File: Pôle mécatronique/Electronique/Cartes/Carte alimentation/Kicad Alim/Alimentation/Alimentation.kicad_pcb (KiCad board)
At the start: 2 copper layers, 68.6 x 78.7 mm, 22 parts, among them J1 Conn_01x04, J2 Conn_01x04, J3 Conn_01x04, J4 Conn_01x05, J5 Conn_01x05, J6 Conn_02x03_Odd_Even, J7 Conn_02x10_Odd_Even, J8 Conn_01x02, J9 Conn_01x02, K1 G5LE-1, Q1 BD135, U1 TSR_2-2450, U2 TSR_2-2450, U3 TSR_2-24120

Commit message: Update HAT + commande
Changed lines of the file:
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@@
   (segment (start 132.842 62.388) (end 143.002 52.228) (width 0.6) (layer "B.Cu") (net 1))
   (segment (start 132.842 72.898) (end 132.842 62.388) (width 0.6) (layer "B.Cu") (net 1))
-  (segment (start 112.522 50.228) (end 104.902 50.228) (width 0.3) (layer "B.Cu") (net 2))
+  (segment (start 112.522 50.228) (end 104.902 50.228) (width 0.5) (layer "B.Cu") (net 2))
   (segment (start 102.172 50.228) (end 102.077 50.133) (width 0.3) (layer "B.Cu") (net 2))
-  (segment (start 134.112 50.228) (end 125.222 50.228) (width 0.3) (layer "B.Cu") (net 2))
-  (segment (start 144.462 50.228) (end 145.542 51.308) (width 0.3) (layer "B.Cu") (net 2))
+  (segment (start 134.112 50.228) (end 125.222 50.228) (width 0.5) (layer "B.Cu") (net 2))
+  (segment (start 144.462 50.228) (end 145.542 51.308) (width 0.5) (layer "B.Cu") (net 2))
   (segment (start 102.077 50.133) (end 97.917 50.133) (width 0.3) (layer "B.Cu") (net 2))
-  (segment (start 145.542 53.213) (end 145.542 51.308) (width 0.3) (layer "B.Cu") (net 2))
-  (segment (start 143.002 50.228) (end 144.462 50.228) (width 0.3) (layer "B.Cu") (net 2))
-  (segment (start 125.222 50.228) (end 112.522 50.228) (width 0.3) (layer "B.Cu") (net 2))
-  (segment (start 143.002 50.228) (end 134.112 50.228) (width 0.3) (layer "B.Cu") (net 2))
+  (segment (start 145.542 53.213) (end 145.542 51.308) (width 0.5) (layer "B.Cu") (net 2))
+  (segment (start 143.002 50.228) (end 144.462 50.228) (width 0.5) (layer "B.Cu") (net 2))
+  (segment (start 125.222 50.228) (end 112.522 50.228) (width 0.5) (layer "B.Cu") (net 2))
+  (segment (start 143.002 50.228) (end 134.112 50.228) (width 0.5) (layer "B.Cu") (net 2))
   (segment (start 102.172 50.228) (end 105.537 50.228) (width 0.3) (layer "B.Cu") (net 2))
-  (segment (start 137.922 72.898) (end 137.922 60.833) (width 0.3) (layer "B.Cu") (net 2))
-  (segment (start 137.922 60.833) (end 145.542 53.213) (width 0.3) (layer "B.Cu") (net 2))
-  (segment (start 134.112 48.228) (end 143.002 48.228) (width 0.3) (layer "B.Cu") (net 3))
+  (segment (start 137.922 72.898) (end 137.922 60.833) (width 0.5) (layer "B.Cu") (net 2))
+  (segment (start 137.922 60.833) (end 145.542 53.213) (width 0.5) (layer "B.Cu") (net 2))
+  (segment (start 134.112 48.228) (end 143.002 48.228) (width 0.5) (layer "B.Cu") (net 3))
   (segment (start 105.442 48.133) (end 105.537 48.228) (width 0.3) (layer "B.Cu") (net 3))
-  (segment (start 146.04201 50.09301) (end 146.04201 53.42011) (width 0.3) (layer "B.Cu") (net 3))
-  (segment (start 125.222 48.228) (end 133.730517 48.228) (width 0.3) (layer "B.Cu") (net 3))
-  (segment (start 140.462 59.00012) (end 140.462 72.898) (width 0.3) (layer "B.Cu") (net 3))
-  (segment (start 125.222 48.228) (end 112.522 48.228) (width 0.3) (layer "B.Cu") (net 3))
-  (segment (start 97.917 48.133) (end 105.442 48.133) (width 0.3) (layer "B.Cu") (net 3))
-  (segment (start 146.04201 53.42011) (end 140.462 59.00012) (width 0.3) (layer "B.Cu") (net 3))
-  (segment (start 133.730517 48.228) (end 134.112 48.228) (width 0.3) (layer "B.Cu") (net 3))
-  (segment (start 144.177 48.228) (end 146.04201 50.09301) (width 0.3) (layer "B.Cu") (net 3))
-  (segment (start 143.002 48.228) (end 144.177 48.228) (width 0.3) (layer "B.Cu") (net 3))
-  (segment (start 104.902 48.228) (end 112.522 48.228) (width 0.3) (layer "B.Cu") (net 3))
+  (segment (start 146.04201 50.09301) (end 146.04201 53.42011) (width 0.5) (layer "B.Cu") (net 3))
+  (segment (start 125.222 48.228) (end 133.730517 48.228) (width 0.5) (layer "B.Cu") (net 3))
+  (segment (start 140.462 59.00012) (end 140.462 72.898) (width 0.5) (layer "B.Cu") (net 3))
+  (segment (start 125.222 48.228) (end 112.522 48.228) (width 0.5) (layer "B.Cu") (net 3))
+  (segment (start 97.917 48.133) (end 105.442 48.133) (width 0.5) (layer "B.Cu") (net 3))
+  (segment (start 146.04201 53.42011) (end 140.462 59.00012) (width 0.5) (layer "B.Cu") (net 3))
+  (segment (start 133.730517 48.228) (end 134.112 48.228) (width 0.5) (layer "B.Cu") (net 3))
+  (segment (start 144.177 48.228) (end 146.04201 50.09301) (width 0.5) (layer "B.Cu") (net 3))
+  (segment (start 143.002 48.228) (end 144.177 48.228) (width 0.5) (layer "B.Cu") (net 3))
+  (segment (start 104.902 48.228) (end 112.522 48.228) (width 0.5) (layer "B.Cu") (net 3))
   (segment (start 130.302 72.898) (end 130.302 56.038) (width 0.6) (layer "B.Cu") (net 5))
   (segment (start 130.302 56.038) (end 134.112 52.228) (width 0.6) (layer "B.Cu") (net 5))
@@
   (segment (start 127.762 54.768) (end 125.222 52.228) (width 0.6) (layer "B.Cu") (net 6))
   (segment (start 120.142 62.103) (end 120.142 67.183) (width 0.6) (layer "F.Cu") (net 7))
-  (via (at 120.142 67.183) (size 0.8) (drill 0.4) (layers "F.Cu" "B.Cu") (net 7))
-  (via (at 120.142 62.103) (size 0.8) (drill 0.4) (layers "F.Cu" "B.Cu") (net 7))
+  (via (at 120.142 67.183) (size 1.6) (drill 0.8) (layers "F.Cu" "B.Cu") (net 7))
+  (via (at 120.142 62.103) (size 1.6) (drill 0.8) (layers "F.Cu" "B.Cu") (net 7))
   (segment (start 120.142 62.103) (end 120.142 61.213) (width 0.6) (layer "B.Cu") (net 7))
   (segment (start 120.142 61.213) (end 118.3645 59.4355) (width 0.6) (layer "B.Cu") (net 7))
@@
   (segment (start 94.647 50.133) (end 94.107 50.673) (width 0.6) (layer "B.Cu") (net 8))
   (segment (start 135.382 67.183) (end 141.732 67.183) (width 0.6) (layer "F.Cu") (net 9))
-  (via (at 135.382 67.183) (size 0.8) (drill 0.4) (layers "F.Cu" "B.Cu") (net 9))
-  (via (at 141.732 67.183) (size 0.8) (drill 0.4) (layers "F.Cu" "B.Cu") (net 9))
+  (via (at 135.382 67.183) (size 1.6) (drill 0.8) (layers "F.Cu" "B.Cu") (net 9))
+  (via (at 141.732 67.183) (size 1.6) (drill 0.8) (layers "F.Cu" "B.Cu") (net 9))
   (segment (start 141.732 67.183) (end 141.732 67.183) (width 0.6) (layer "B.Cu") (net 9))
   (segment (start 141.732 59.563) (end 147.447 53.848) (width 0.6) (layer "B.Cu") (net 9))

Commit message: Update alim sécurité
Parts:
- added F1: 2A, Fuse:Fuse_BelFuse_0ZRE0012FF_L8.3mm_W3.8mm, F.Cu at (138.5, 97.5)
- added F2: 2A, Fuse:Fuse_BelFuse_0ZRE0012FF_L8.3mm_W3.8mm, F.Cu at (134.1, 99.1)
- added F3: 2A, Fuse:Fuse_BelFuse_0ZRE0012FF_L8.3mm_W3.8mm, F.Cu at (118.9, 97.5)
- added SW1: SW_DPDT_x2, Autre:Switch_3_Pin, F.Cu at (101.7, 100.2)
- J8: value Conn_01x02 -> 24V in
- J9: value Conn_01x02 -> 24V out
- moved J9 32.7 mm to (96.9, 109.1)
- moved J8 22.3 mm to (127.3, 109.1)
- moved REF** 11.4 mm to (90.9, 95.8)
- moved REF** 4.02 mm to (148.1, 111.0)
- moved REF** 2.29 mm to (148.1, 40.5)
- moved REF** 1.91 mm to (90.9, 40.5)
- moved K1 1.27 mm to (103.6, 75.4)
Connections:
- J9 pad 2: Vbatt -> VbattRelay
- K1 pad 3: unconnected-(K1-Pad3) -> Net-(K1-Pad3)
- K1 pad 4: VbattProtected -> Net-(K1-Pad4)
- U1 pad 1: Vbatt -> Net-(U1-Pad1)
- U2 pad 1: Vbatt -> Net-(U2-Pad1)
- U3 pad 1: VbattProtected -> Net-(U3-Pad1)
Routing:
- net VbattRelay: track 0.00 -> 33.9 mm
- net Vbatt: track 84.8 -> 114.8 mm
- net Net-(K1-Pad4): track 0.00 -> 12.2 mm
- net VbattProtected: track 10.8 -> 0.00 mm
- net Net-(K1-Pad3): track 0.00 -> 10.6 mm
- net Net-(U2-Pad1): track 0.00 -> 9.00 mm
- net Net-(U1-Pad1): track 0.00 -> 6.34 mm
- net Net-(U3-Pad1): track 0.00 -> 5.81 mm
- net GND: track 0.00 -> 3.81 mm, vias 0 -> 2
- net 5Vout5: track 28.6 -> 30.9 mm
- net 12V: track 34.3 -> 32.7 mm
- net can_L: track 73.5 -> 72.6 mm
- net Net-(D1-Pad2): track 17.1 -> 17.6 mm
- removed copper zone on F.Cu, net GND
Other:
- board size 68.6 x 78.7 mm -> 67.3 x 80.6 mm
- board text removed: "Batterie"

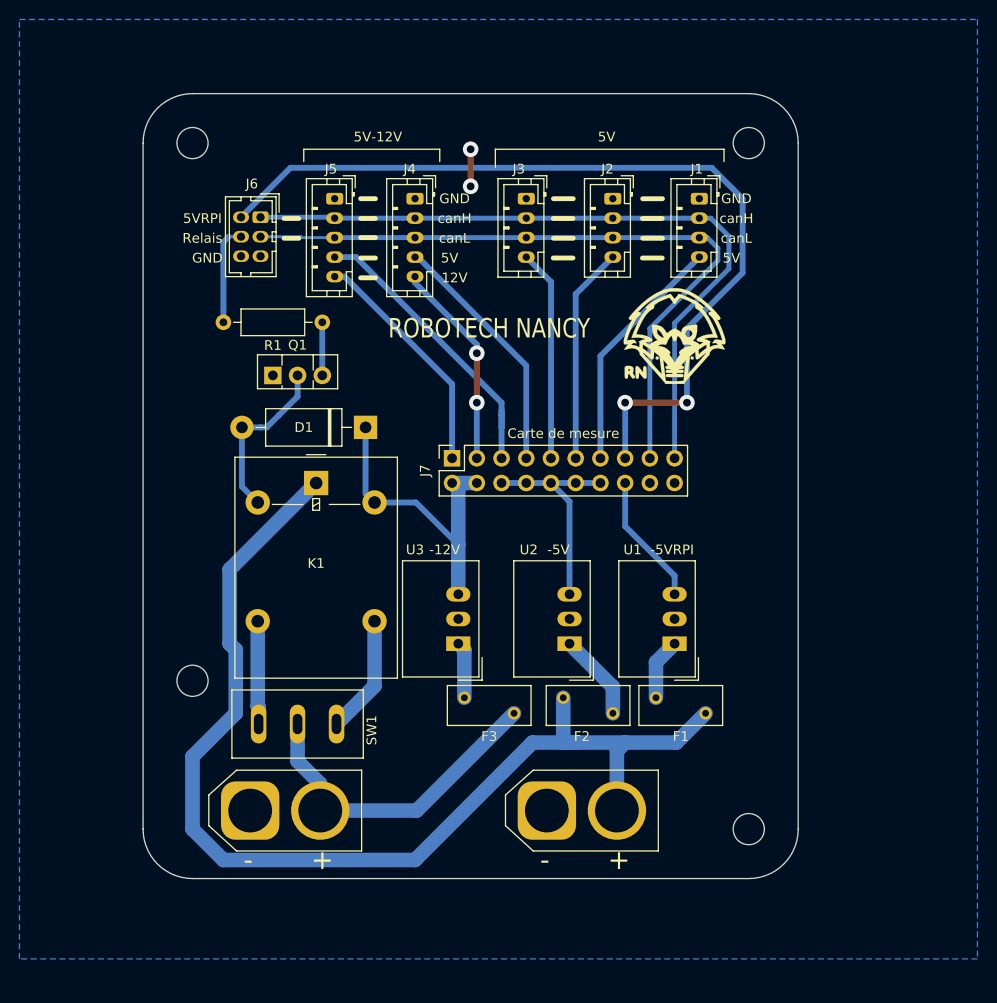
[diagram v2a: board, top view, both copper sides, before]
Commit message: Update Alim
Fusible
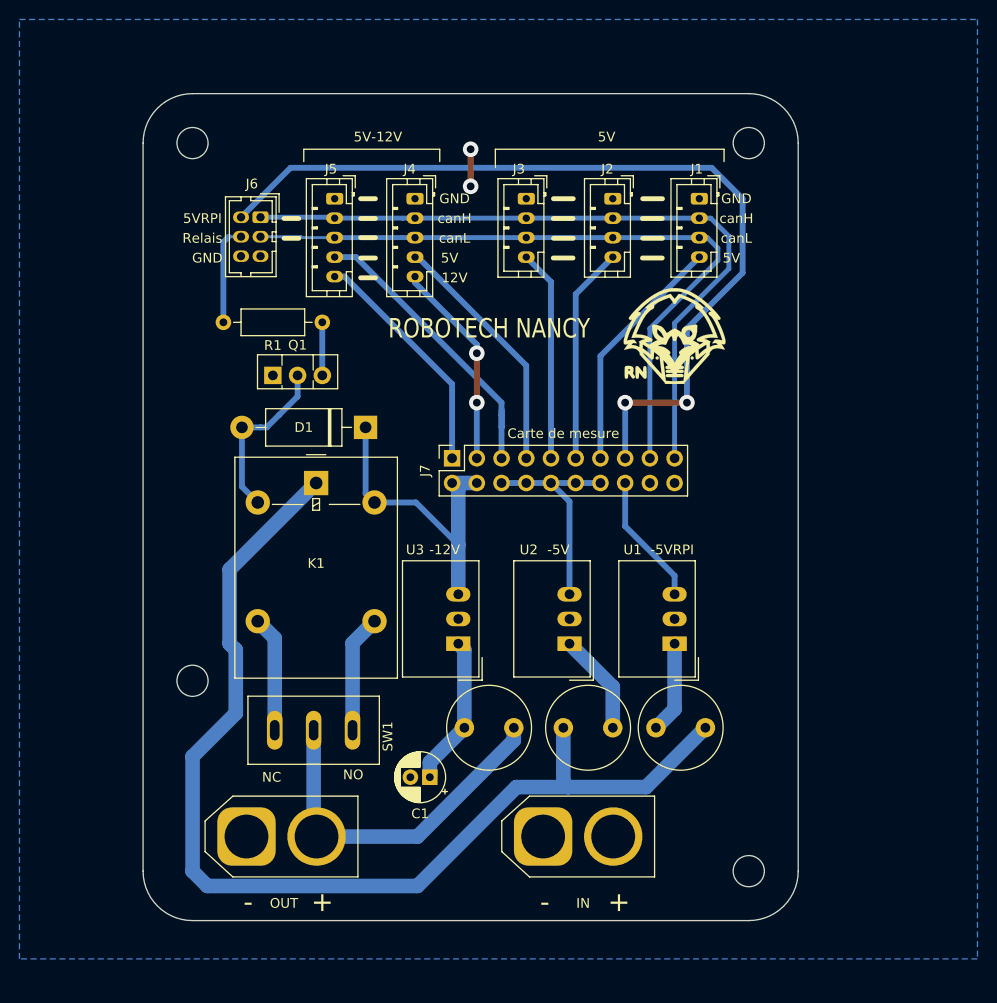
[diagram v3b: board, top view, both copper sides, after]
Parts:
- added C1: 22uF, Capacitor_THT:CP_Radial_D5.0mm_P2.00mm, F.Cu at (115.3, 105.7)
- F1, F2, F3: value 2A -> 500mA; footprint Fuse:Fuse_BelFuse_0ZRE0012FF_L8.3mm_W3.8mm -> Fuse:Fuse_Littelfuse_372_D8.50mm
- moved REF** 4.32 mm to (148.1, 115.3)
- moved F1 3.09 mm to (138.5, 100.6)
- moved F3 3.09 mm to (118.9, 100.6)
- moved J8 2.69 mm to (127.0, 111.8)
- moved J9 2.69 mm to (96.5, 111.8)
- moved SW1 1.77 mm to (103.4, 100.8)
- moved F2 1.49 mm to (134.1, 100.6)
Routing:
- net Net-(F3-Pad1): track 5.81 -> 15.4 mm
- net Net-(F1-Pad1): track 6.34 -> 9.43 mm
- net Vbatt: track 114.8 -> 112.0 mm
- net VbattRelay: track 33.9 -> 36.7 mm
- net Net-(F2-Pad1): track 9.00 -> 10.5 mm
- net Net-(K1-Pad3): track 10.6 -> 11.9 mm
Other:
- board size 67.3 x 80.6 mm -> 67.3 x 85 mm
- board text added: "IN"
- board text added: "NC"
- board text added: "NO"
- board text added: "OUT"

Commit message: Update Alim
Changement des dimensions
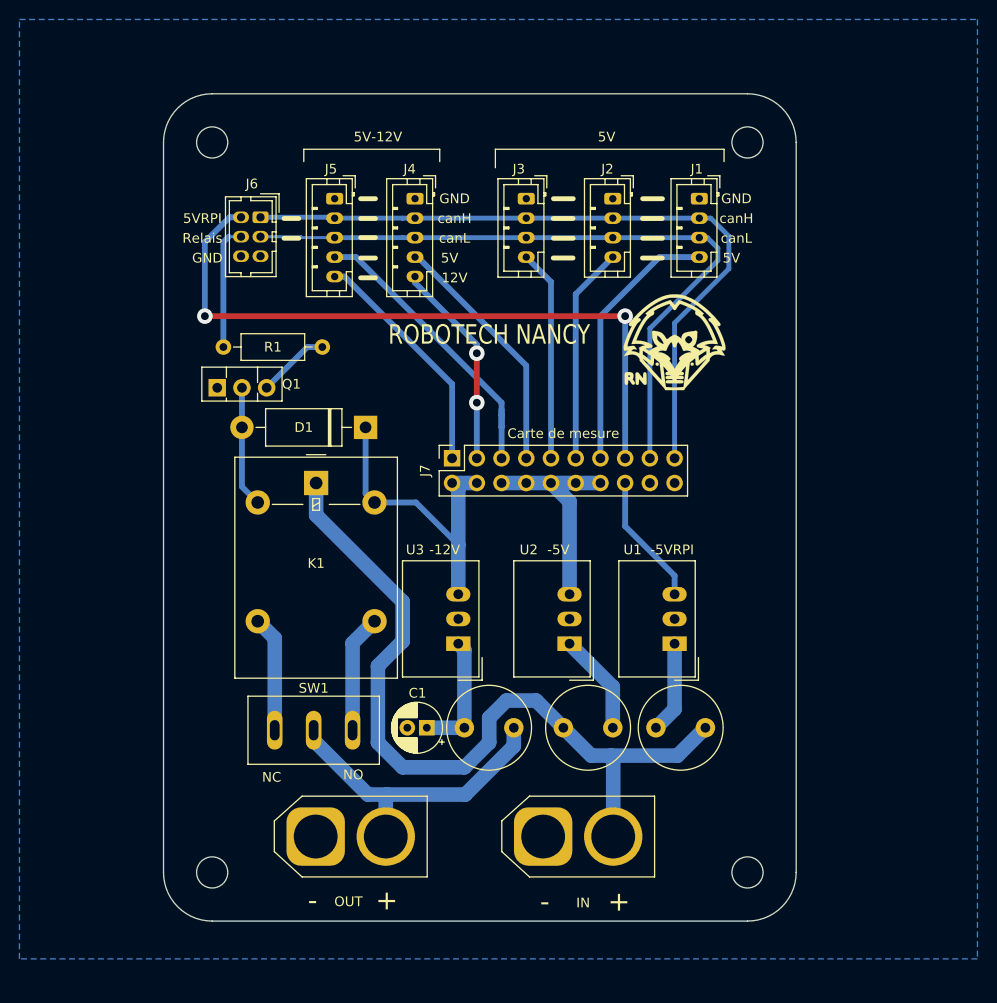
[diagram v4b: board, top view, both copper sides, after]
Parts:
- moved REF** 19.8 mm to (93.0, 115.4)
- moved J9 7.11 mm to (103.6, 111.8)
- moved Q1 5.85 mm to (93.5, 65.7)
- moved C1 5.09 mm to (115.0, 100.6)
- moved R1 2.54 mm to (104.3, 61.5)
- moved REF** 2.02 mm to (93.0, 40.4)
- moved G*** 0.63 mm to (140.5, 60.8) (x2)
- moved REF** 0.19 mm to (148.0, 115.4)
- moved REF** 0.15 mm to (148.0, 40.4)
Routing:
- net Vbatt: track 112.0 -> 82.4 mm
- net 5VRPI: track 90.3 -> 70.2 mm
- net 5V: track 22.4 -> 32.5 mm
- net Net-(D1-Pad2): track 17.6 -> 12.5 mm
- net VbattRelay: track 36.7 -> 32.2 mm
- net GND: track 3.81 -> 0.00 mm, vias 2 -> 0
- net Net-(F3-Pad1): track 15.4 -> 12.8 mm
- net cmd_relais: track 10.3 -> 12.8 mm
- net 5Vout1: track 24.9 -> 27.3 mm
- net Net-(Q1-Pad3): track 5.45 -> 7.45 mm
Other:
- board size 67.3 x 85 mm -> 65 x 85 mm

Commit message: Update HAT
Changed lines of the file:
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@@
   (segment (start 120.142 72.898) (end 120.142 67.183) (width 0.6) (layer "B.Cu") (net 7))
   (segment (start 118.3645 59.4355) (end 113.792 54.863) (width 0.6) (layer "B.Cu") (net 7))
-  (segment (start 94.647 50.133) (end 95.917 50.133) (width 0.3) (layer "B.Cu") (net 8))
-  (segment (start 94.107 50.673) (end 94.647 50.133) (width 0.6) (layer "B.Cu") (net 8))
   (segment (start 94.107 61.468) (end 94.107 50.673) (width 0.6) (layer "B.Cu") (net 8))
+  (segment (start 94.647 50.133) (end 94.107 50.673) (width 0.5) (layer "B.Cu") (net 8))
+  (segment (start 95.917 50.133) (end 94.647 50.133) (width 0.5) (layer "B.Cu") (net 8))
   (segment (start 135.382 58.293) (end 92.202 58.293) (width 0.6) (layer "F.Cu") (net 9))
   (via (at 135.382 58.293) (size 1.6) (drill 0.8) (layers "F.Cu" "B.Cu") (net 9))

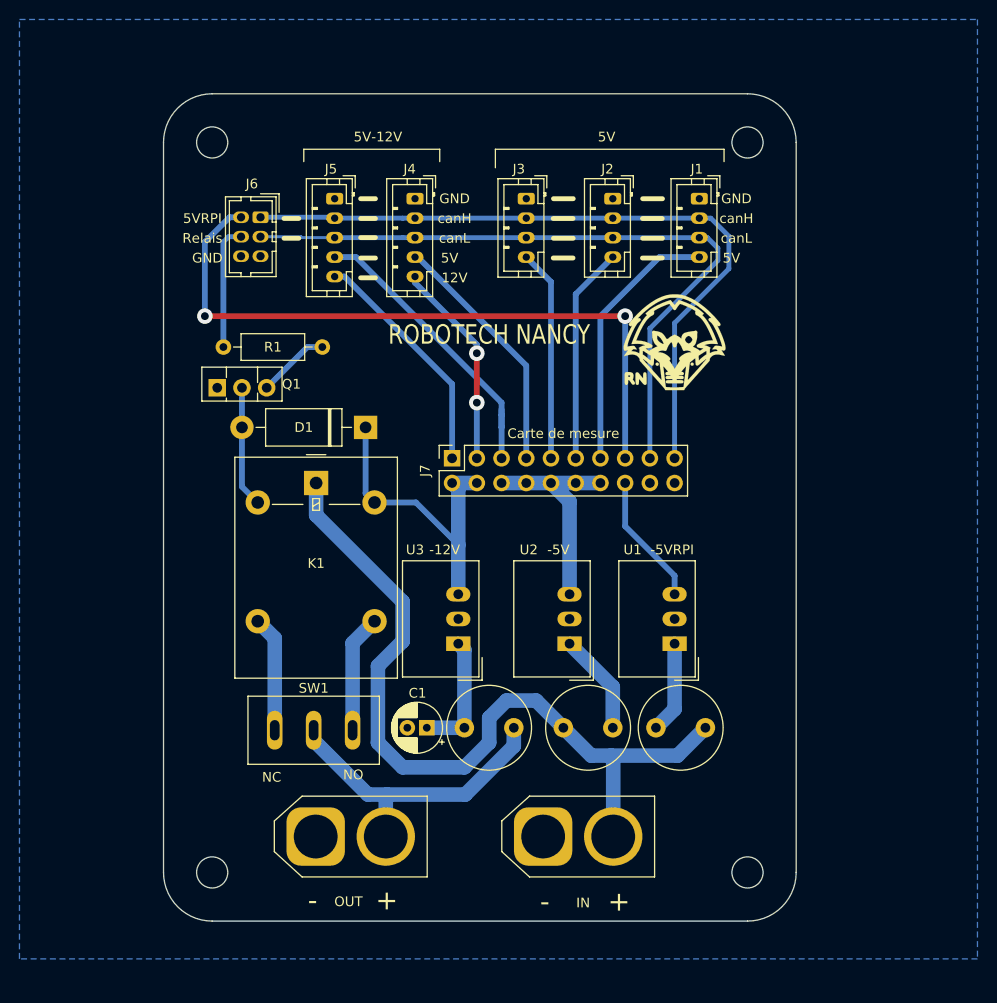
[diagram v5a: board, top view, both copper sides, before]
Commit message: Update fabrication
Pistes et pastilles plus larges
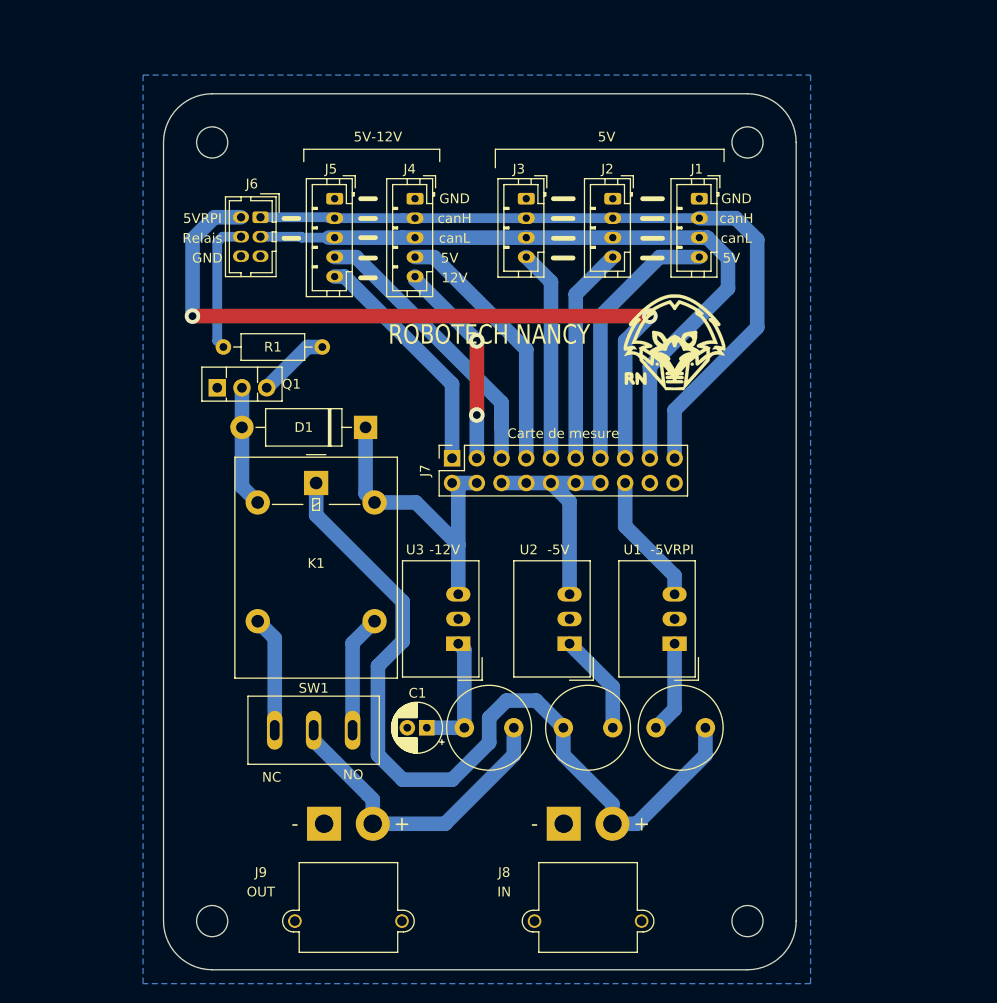
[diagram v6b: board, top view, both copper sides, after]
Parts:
- J8, J9: footprint Connector_AMASS:AMASS_XT60-F_1x02_P7.20mm_Vertical -> Connector_AMASS:AMASS_XT30PW-M_1x02_P2.50mm_Horizontal
- moved REF** 5.00 mm to (93.0, 120.4)
- moved REF** 5.00 mm to (148.0, 120.4)
- moved J8 2.49 mm to (129.1, 110.4), turned to 180 degrees
- moved J9 1.57 mm to (104.5, 110.4), turned to 180 degrees
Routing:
- net 5VRPI: track 70.2 -> 76.5 mm
- net can_H: track 74.7 -> 78.6 mm
- net Vbatt: track 82.4 -> 86.0 mm
- net 5Vout4: track 25.6 -> 26.5 mm
- net cmd_relais: track 12.8 -> 13.7 mm
- net can_L: track 72.6 -> 73.5 mm
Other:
- board size 65 x 85 mm -> 65 x 90 mm
- board text removed: "+"
- board text removed: "-"
